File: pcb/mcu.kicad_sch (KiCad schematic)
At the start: 15 parts, among them J301 Conn_02x07_Top_Bottom, J302 1658525-9, U301 EFM32GG990F1024, Y301 Crystal_GND24

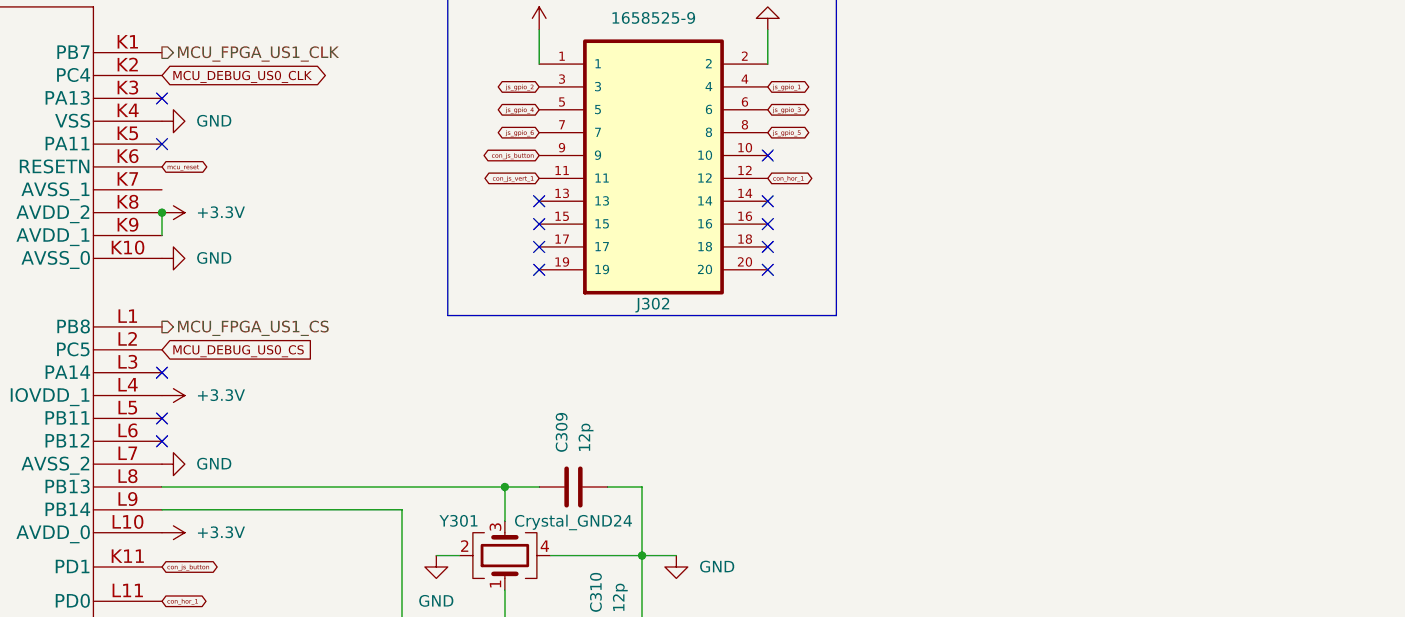
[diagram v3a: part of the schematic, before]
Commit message: add footprints + fix unnconnected
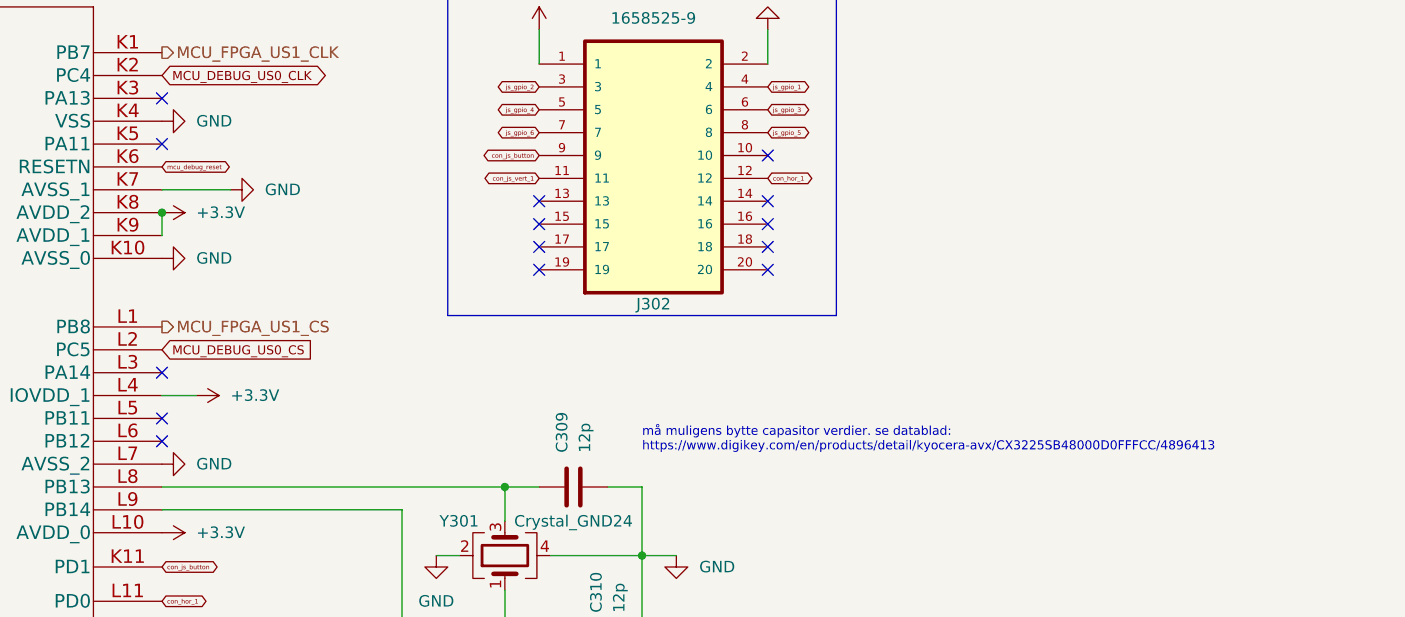
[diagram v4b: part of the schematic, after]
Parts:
- J301: footprint (none) -> Connector_PinHeader_2.54mm:PinHeader_2x07_P2.54mm_Vertical
- Y301: footprint (none) -> oscillator-footprints:OSC_ECS-2520S25-250-FN-TR
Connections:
- net GND: now also U301.K7 (AVSS_1)
- net mcu_reset renamed mcu_debug_reset
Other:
- note added: "må muligens bytte capasitor verdier. se datablad: https://www.digikey.com/en/products/detail/kyocera-avx/CX3225SB48000D0FFFCC/4896413"
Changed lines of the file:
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@@
+    (stroke (width 0) (type default) (color 0 0 0 0))
+  )
+  (wire (pts (xy 201.93 74.93) (xy 198.12 74.93))
     (stroke (width 0) (type default) (color 0 0 0 0))
   )
@@
   )
   (wire (pts (xy 224.79 102.87) (xy 236.22 102.87))
+    (stroke (width 0) (type default) (color 0 0 0 0))
+  )
+  (wire (pts (xy 198.12 52.07) (xy 205.74 52.07))
     (stroke (width 0) (type default) (color 0 0 0 0))
   )
@@
   (text "Controler headers" (at 231.14 25.4 0)
     (effects (font (size 1.27 1.27)) (justify left bottom))
+  )
+  (text "må muligens bytte capasitor verdier. se datablad:\nhttps://www.digikey.com/en/products/detail/kyocera-avx/CX3225SB48000D0FFFCC/4896413"
+    (at 251.46 81.28 0)
+    (effects (font (size 1 1)) (justify left bottom))
   )
   (text "MCU clock out" (at 115.57 33.02 0)
@@
     )
   )
+  (global_label "mcu_debug_reset" (shape bidirectional) (at 198.12 49.53 0) (fields_autoplaced)
+    (effects (font (size 0.5 0.5)) (justify left))
+    (property "Intersheet References" "${INTERSHEET_REFS}" (id 0) (at 205.4748 49.4988 0)
+      (effects (font (size 0.5 0.5)) (justify left) hide)
+    )
+  )
   (global_label "MCU_DEBUG_US0_MOSI" (shape input) (at 118.11 152.4 0) (fields_autoplaced)
     (effects (font (size 1 1)) (justify left))
@@
     )
   )
-  (global_label "mcu_reset" (shape bidirectional) (at 198.12 49.53 0) (fields_autoplaced)
-    (effects (font (size 0.5 0.5)) (justify left))
-    (property "Intersheet References" "${INTERSHEET_REFS}" (id 0) (at 202.8557 49.4988 0)
-      (effects (font (size 0.5 0.5)) (justify left) hide)
-    )
-  )
   (global_label "js_gpio_5" (shape bidirectional) (at 147.32 105.41 180) (fields_autoplaced)
     (effects (font (size 0.8 0.8)) (justify right))
@@
     )
     (property "Datasheet" "~" (id 3) (at 113.03 100.33 0)
+      (effects (font (size 1.27 1.27)) hide)
+    )
+    (pin "1")
+  )
+  (symbol (lib_id "power:GND") (at 205.74 52.07 90) (unit 1)
+    (in_bom yes) (on_board yes) (fields_autoplaced)
+    (property "Reference" "#PWR0101" (id 0) (at 212.09 52.07 0)
+      (effects (font (size 1.27 1.27)) hide)
+    )
+    (property "Value" "GND" (id 1) (at 209.55 52.0699 90)
+      (effects (font (size 1.27 1.27)) (justify right))
+    )
+    (property "Footprint" "" (id 2) (at 205.74 52.07 0)
+      (effects (font (size 1.27 1.27)) hide)
+    )
+    (property "Datasheet" "" (id 3) (at 205.74 52.07 0)
       (effects (font (size 1.27 1.27)) hide)
     )
@@
     (pin "2")
   )
-  (symbol (lib_id "power:+3.3V") (at 198.12 74.93 270) (unit 1)
-    (in_bom yes) (on_board yes) (fields_autoplaced)
-    (property "Reference" "#PWR0317" (id 0) (at 194.31 74.93 0)
-      (effects (font (size 1.27 1.27)) hide)
-    )
-    (property "Value" "+3.3V" (id 1) (at 201.93 74.9299 90)
-      (effects (font (size 1.27 1.27)) (justify left))
-    )
-    (property "Footprint" "" (id 2) (at 198.12 74.93 0)
-      (effects (font (size 1.27 1.27)) hide)
-    )
-    (property "Datasheet" "" (id 3) (at 198.12 74.93 0)
+  (symbol (lib_id "power:+3.3V") (at 201.93 74.93 270) (unit 1)
+    (in_bom yes) (on_board yes) (fields_autoplaced)
+    (property "Reference" "#PWR0317" (id 0) (at 198.12 74.93 0)
+      (effects (font (size 1.27 1.27)) hide)
+    )
+    (property "Value" "+3.3V" (id 1) (at 205.74 74.9299 90)
+      (effects (font (size 1.27 1.27)) (justify left))
+    )
+    (property "Footprint" "" (id 2) (at 201.93 74.93 0)
+      (effects (font (size 1.27 1.27)) hide)
+    )
+    (property "Datasheet" "" (id 3) (at 201.93 74.93 0)
       (effects (font (size 1.27 1.27)) hide)
     )
@@
     (property "Reference" "J301" (id 0) (at 111.76 140.97 0))
     (property "Value" "Conn_02x07_Top_Bottom" (id 1) (at 111.76 143.51 0))
-    (property "Footprint" "" (id 2) (at 110.49 154.94 0)
+    (property "Footprint" "Connector_PinHeader_2.54mm:PinHeader_2x07_P2.54mm_Vertical" (id 2) (at 110.49 154.94 0)
       (effects (font (size 1.27 1.27)) hide)
     )
@@
     (property "Reference" "Y301" (id 0) (at 231.14 88.9 90))
     (property "Value" "Crystal_GND24" (id 1) (at 243.84 88.9 90))
-    (property "Footprint" "" (id 2) (at 236.22 92.71 0)
-      (effects (font (size 1.27 1.27)) hide)
-    )
+    (property "Footprint" "oscillator-footprints:OSC_ECS-2520S25-250-FN-TR" (id 2) (at 236.22 92.71 0)
+      (effects (font (size 1.27 1.27)) hide)
+    )

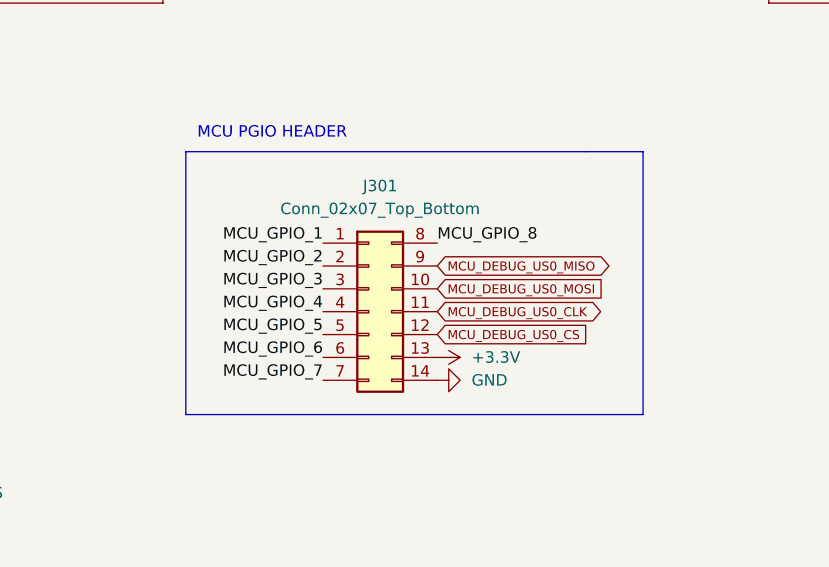
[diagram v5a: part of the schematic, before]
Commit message: change footprint of connector
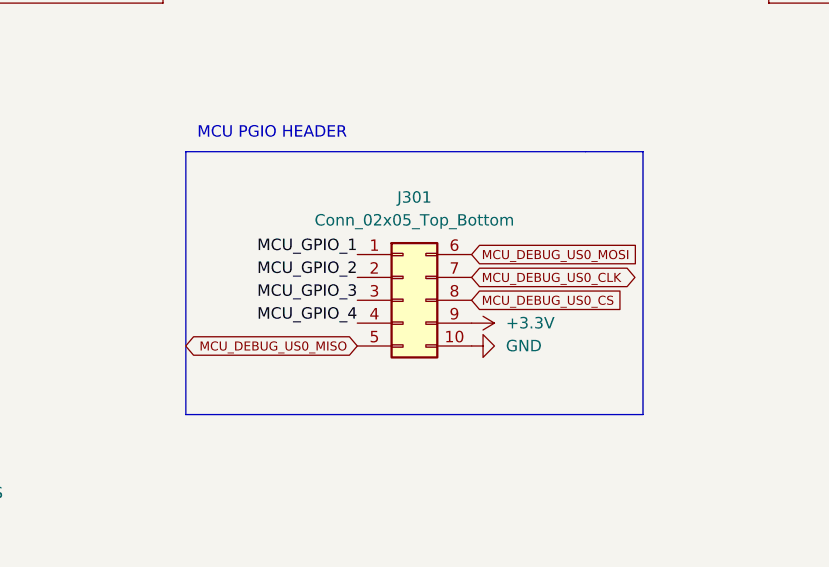
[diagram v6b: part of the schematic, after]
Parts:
- removed J301: Conn_02x07_Top_Bottom, Connector_PinHeader_2.54mm:PinHeader_2x07_P2.54mm_Vertical, symbol Connector_Generic:Conn_02x07_Top_Bottom
- added J301: Conn_02x05_Top_Bottom, Connector_PinHeader_2.54mm:PinHeader_2x05_P2.54mm_Vertical, symbol Connector_Generic:Conn_02x05_Top_Bottom
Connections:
- net +3.3V: now also J301.9 (Pin_9)
- net GND: now also J301.10 (Pin_10)
- net MCU_DEBUG_US0_CLK: now also J301.7 (Pin_7)
- net MCU_DEBUG_US0_CS: now also J301.8 (Pin_8)
- net MCU_DEBUG_US0_MISO: now also J301.5 (Pin_5)
- net MCU_DEBUG_US0_MOSI: now also J301.6 (Pin_6)
- net MCU_GPIO_1: now also J301.1 (Pin_1)
- net MCU_GPIO_2: now also J301.2 (Pin_2)
- net MCU_GPIO_3: now also J301.3 (Pin_3)
- net MCU_GPIO_4: now also J301.4 (Pin_4)
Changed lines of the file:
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@@
     (effects (font (size 1.27 1.27)) (justify left bottom))
+  )
+  (label "MCU_GPIO_4" (at 109.22 156.21 180)
+    (effects (font (size 1.27 1.27)) (justify right bottom))
   )
   (label "MCU_GPIO_4" (at 34.29 97.79 180)
@@
     (effects (font (size 1 1)) (justify right bottom))
   )
-  (label "MCU_GPIO_6" (at 105.41 160.02 180)
-    (effects (font (size 1.27 1.27)) (justify right bottom))
-  )
-  (label "MCU_GPIO_4" (at 105.41 154.94 180)
-    (effects (font (size 1.27 1.27)) (justify right bottom))
-  )
   (label "MCU_GPIO_9" (at 95.25 64.77 0)
     (effects (font (size 1.27 1.27)) (justify left bottom))
   )
-  (label "MCU_GPIO_3" (at 105.41 152.4 180)
+  (label "MCU_GPIO_3" (at 109.22 153.67 180)
     (effects (font (size 1.27 1.27)) (justify right bottom))
   )
@@
     (effects (font (size 1.27 1.27)) (justify left bottom))
   )
-  (label "MCU_GPIO_1" (at 105.41 147.32 180)
-    (effects (font (size 1.27 1.27)) (justify right bottom))
-  )
-  (label "MCU_GPIO_7" (at 105.41 162.56 180)
+  (label "MCU_GPIO_1" (at 109.22 148.59 180)
     (effects (font (size 1.27 1.27)) (justify right bottom))
   )
@@
     (effects (font (size 1.27 1.27)) (justify left bottom))
   )
-  (label "MCU_GPIO_5" (at 105.41 157.48 180)
-    (effects (font (size 1.27 1.27)) (justify right bottom))
-  )
   (label "MCU_GPIO_11" (at 95.25 72.39 0)
     (effects (font (size 1.27 1.27)) (justify left bottom))
@@
     (effects (font (size 1.27 1.27)) (justify right bottom))
   )
-  (label "MCU_GPIO_2" (at 105.41 149.86 180)
+  (label "MCU_GPIO_2" (at 109.22 151.13 180)
     (effects (font (size 1.27 1.27)) (justify right bottom))
   )
@@
     (effects (font (size 1.27 1.27)) (justify left bottom))
   )
-  (label "MCU_GPIO_8" (at 118.11 147.32 0)
-    (effects (font (size 1.27 1.27)) (justify left bottom))
-  )
-  (global_label "MCU_DEBUG_US0_CS" (shape input) (at 118.11 157.48 0) (fields_autoplaced)
+  (global_label "MCU_DEBUG_US0_CS" (shape input) (at 121.92 153.67 0) (fields_autoplaced)
     (effects (font (size 1 1)) (justify left))
-    (property "Intersheet References" "${INTERSHEET_REFS}" (id 0) (at 135.3433 157.4175 0)
+    (property "Intersheet References" "${INTERSHEET_REFS}" (id 0) (at 139.1533 153.6075 0)
       (effects (font (size 1 1)) (justify left) hide)
     )
@@
     )
   )
-  (global_label "MCU_DEBUG_US0_MOSI" (shape input) (at 118.11 152.4 0) (fields_autoplaced)
+  (global_label "MCU_DEBUG_US0_MOSI" (shape input) (at 121.92 148.59 0) (fields_autoplaced)
     (effects (font (size 1 1)) (justify left))
-    (property "Intersheet References" "${INTERSHEET_REFS}" (id 0) (at 137.01 152.4625 0)
+    (property "Intersheet References" "${INTERSHEET_REFS}" (id 0) (at 140.82 148.6525 0)
       (effects (font (size 1 1)) (justify left) hide)
     )
@@
     )
   )
-  (global_label "MCU_DEBUG_US0_CLK" (shape bidirectional) (at 118.11 154.94 0) (fields_autoplaced)
+  (global_label "MCU_DEBUG_US0_CLK" (shape bidirectional) (at 121.92 151.13 0) (fields_autoplaced)
     (effects (font (size 1 1)) (justify left))
-    (property "Intersheet References" "${INTERSHEET_REFS}" (id 0) (at 136.2005 154.8775 0)
+    (property "Intersheet References" "${INTERSHEET_REFS}" (id 0) (at 140.0105 151.0675 0)
       (effects (font (size 1 1)) (justify left) hide)
     )
@@
     )
   )
+  (global_label "MCU_DEBUG_US0_MISO" (shape bidirectional) (at 109.22 158.75 180) (fields_autoplaced)
+    (effects (font (size 1 1)) (justify right))
+    (property "Intersheet References" "${INTERSHEET_REFS}" (id 0) (at 90.32 158.6875 0)
+      (effects (font (size 1 1)) (justify right) hide)
+    )
+  )
   (global_label "con_js_vert_1" (shape bidirectional) (at 240.03 50.8 180) (fields_autoplaced)
     (effects (font (size 0.5 0.5)) (justify right))
@@
     (property "Intersheet References" "${INTERSHEET_REFS}" (id 0) (at 141.37 112.9988 0)
       (effects (font (size 0.5 0.5)) (justify right) hide)
-    )
-  )
-  (global_label "MCU_DEBUG_US0_MISO" (shape bidirectional) (at 118.11 149.86 0) (fields_autoplaced)
-    (effects (font (size 1 1)) (justify left))
-    (property "Intersheet References" "${INTERSHEET_REFS}" (id 0) (at 137.01 149.9225 0)
-      (effects (font (size 1 1)) (justify left) hide)
     )
   )
@@
     (pin "2")
   )
-  (symbol (lib_id "power:+3.3V") (at 118.11 160.02 270) (unit 1)
-    (in_bom yes) (on_board yes) (fields_autoplaced)
-    (property "Reference" "#PWR0307" (id 0) (at 114.3 160.02 0)
-      (effects (font (size 1.27 1.27)) hide)
-    )
-    (property "Value" "+3.3V" (id 1) (at 121.92 160.0199 90)
-      (effects (font (size 1.27 1.27)) (justify left))
-    )
-    (property "Footprint" "" (id 2) (at 118.11 160.02 0)
-      (effects (font (size 1.27 1.27)) hide)
-    )
-    (property "Datasheet" "" (id 3) (at 118.11 160.02 0)
+  (symbol (lib_id "power:+3.3V") (at 121.92 156.21 270) (unit 1)
+    (in_bom yes) (on_board yes) (fields_autoplaced)
+    (property "Reference" "#PWR0307" (id 0) (at 118.11 156.21 0)
+      (effects (font (size 1.27 1.27)) hide)
+    )
+    (property "Value" "+3.3V" (id 1) (at 125.73 156.2099 90)
+      (effects (font (size 1.27 1.27)) (justify left))
+    )
+    (property "Footprint" "" (id 2) (at 121.92 156.21 0)
+      (effects (font (size 1.27 1.27)) hide)
+    )
+    (property "Datasheet" "" (id 3) (at 121.92 156.21 0)
       (effects (font (size 1.27 1.27)) hide)
     )
@@
     (pin "1")
   )
-  (symbol (lib_id "Connector_Generic:Conn_02x07_Top_Bottom") (at 110.49 154.94 0) (unit 1)
-    (in_bom yes) (on_board yes) (fields_autoplaced)
-    (property "Reference" "J301" (id 0) (at 111.76 140.97 0))
-    (property "Value" "Conn_02x07_Top_Bottom" (id 1) (at 111.76 143.51 0))
-    (property "Footprint" "Connector_PinHeader_2.54mm:PinHeader_2x07_P2.54mm_Vertical" (id 2) (at 110.49 154.94 0)
-      (effects (font (size 1.27 1.27)) hide)
-    )
-    (property "Datasheet" "~" (id 3) (at 110.49 154.94 0)
+  (symbol (lib_id "Connector_Generic:Conn_02x05_Top_Bottom") (at 114.3 153.67 0) (unit 1)
+    (in_bom yes) (on_board yes) (fields_autoplaced)
+    (property "Reference" "J301" (id 0) (at 115.57 142.24 0))
+    (property "Value" "Conn_02x05_Top_Bottom" (id 1) (at 115.57 144.78 0))
+    (property "Footprint" "Connector_PinHeader_2.54mm:PinHeader_2x05_P2.54mm_Vertical" (id 2) (at 114.3 153.67 0)
+      (effects (font (size 1.27 1.27)) hide)
+    )
+    (property "Datasheet" "~" (id 3) (at 114.3 153.67 0)
       (effects (font (size 1.27 1.27)) hide)
     )
     (pin "1")
     (pin "10")
-    (pin "11")
-    (pin "12")
-    (pin "13")
-    (pin "14")
     (pin "2")
     (pin "3")
@@
     (pin "9")
   )
-  (symbol (lib_id "power:GND") (at 118.11 162.56 90) (unit 1)
-    (in_bom yes) (on_board yes) (fields_autoplaced)
-    (property "Reference" "#PWR0308" (id 0) (at 124.46 162.56 0)
-      (effects (font (size 1.27 1.27)) hide)
-    )
-    (property "Value" "GND" (id 1) (at 121.92 162.5599 90)
+  (symbol (lib_id "power:GND") (at 121.92 158.75 90) (unit 1)
+    (in_bom yes) (on_board yes) (fields_autoplaced)
+    (property "Reference" "#PWR0308" (id 0) (at 128.27 158.75 0)
+      (effects (font (size 1.27 1.27)) hide)
+    )
+    (property "Value" "GND" (id 1) (at 125.73 158.7499 90)
       (effects (font (size 1.27 1.27)) (justify right))
     )
-    (property "Footprint" "" (id 2) (at 118.11 162.56 0)
-      (effects (font (size 1.27 1.27)) hide)
-    )
-    (property "Datasheet" "" (id 3) (at 118.11 162.56 0)
-      (effects (font (size 1.27 1.27)) hide)
-    )
+    (property "Footprint" "" (id 2) (at 121.92 158.75 0)
+      (effects (font (size 1.27 1.27)) hide)
+    )
+    (property "Datasheet" "" (id 3) (at 121.92 158.75 0)
+      (effects (font (size 1.27 1.27)) hide)
+    )
